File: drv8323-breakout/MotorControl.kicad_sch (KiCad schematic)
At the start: 24 parts, among them U1 DRV8323HRTAR, U2 CSD18534Q5A, U3 CSD18534Q5A, U4 CSD18534Q5A, U5 CSD18534Q5A, U6 CSD18534Q5A, U7 CSD18534Q5A

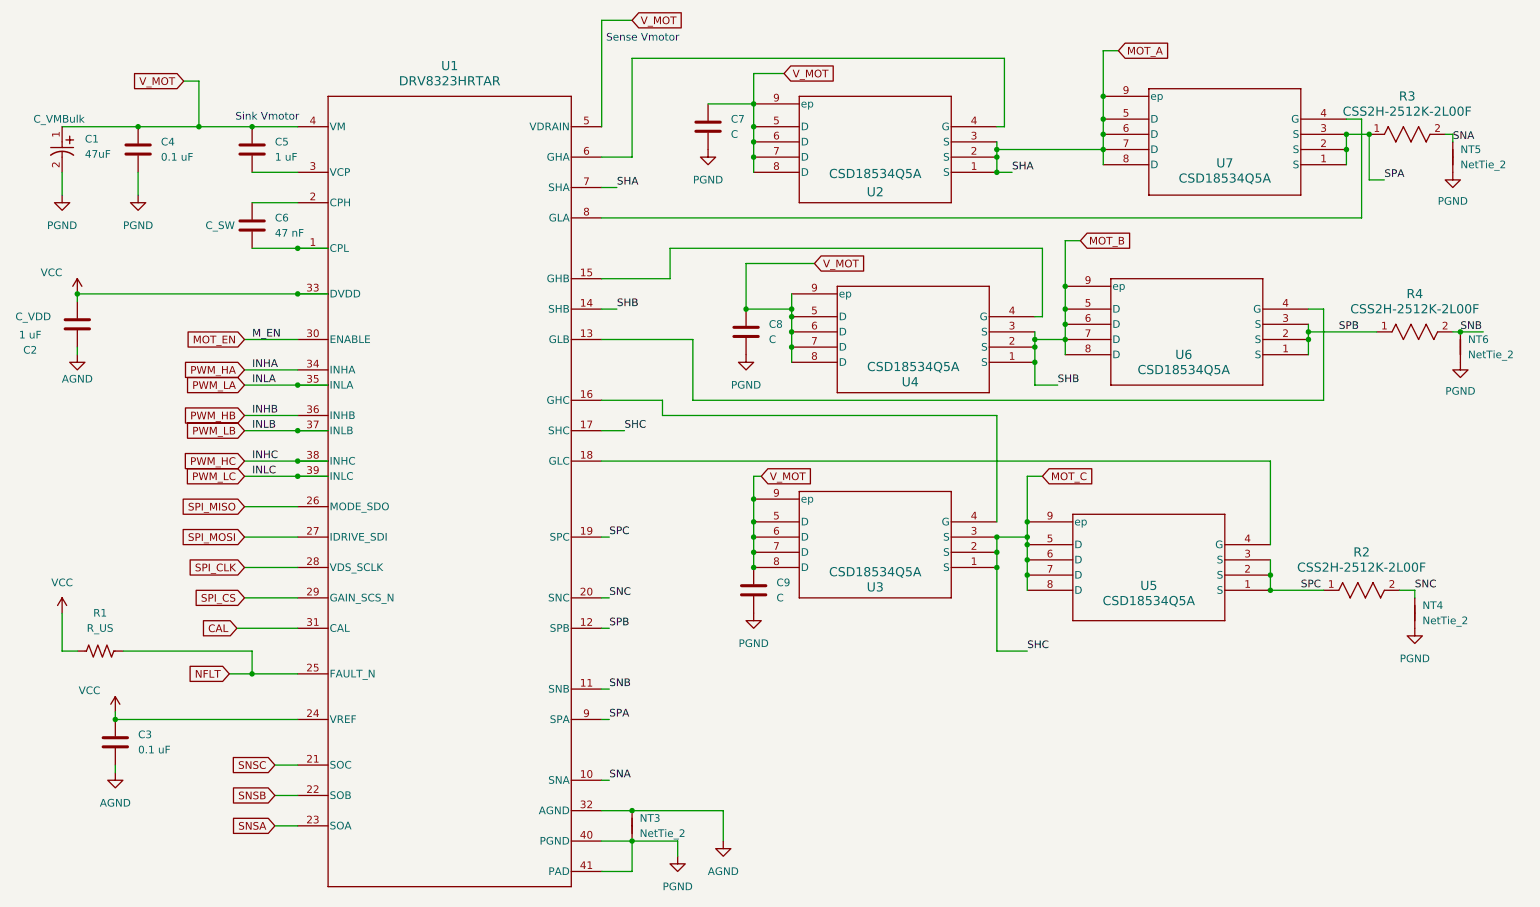
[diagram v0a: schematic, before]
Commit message: updated symbols for sanity and PCB for mfg, no DRC errors, only net type ERC errors
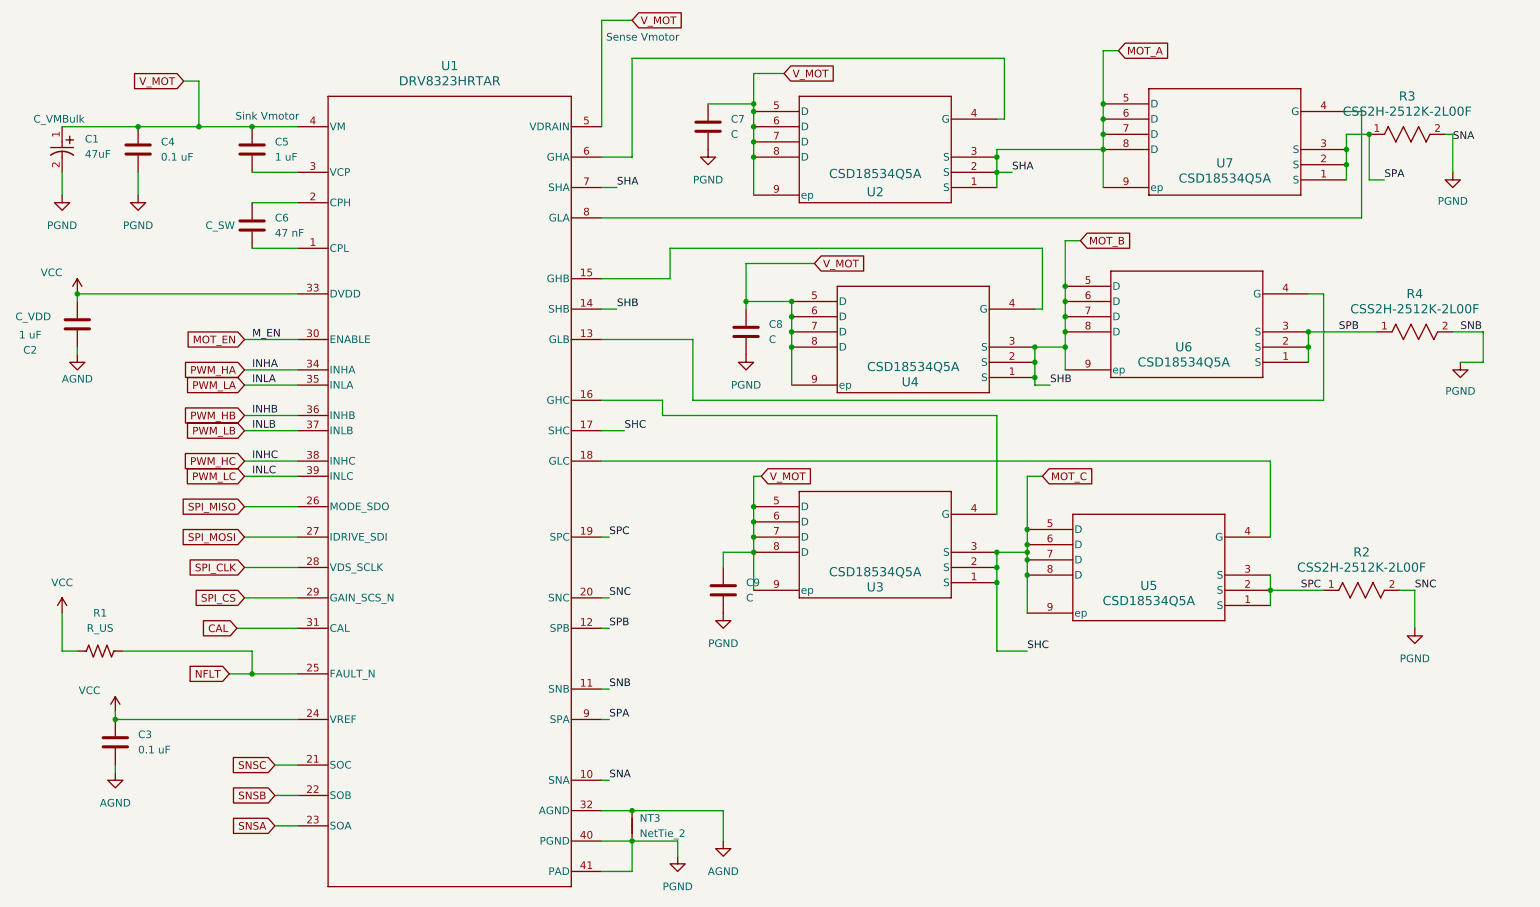
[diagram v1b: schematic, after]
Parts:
- removed NT4, NT5, NT6: NetTie_2, symbol Device:NetTie_2
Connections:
- net SNA is gone; now on net PGND: R3.2, U1.10 (SNA)
- net SNB is gone; now on net PGND: R4.2, U1.11 (SNB)
- net SNC is gone; now on net PGND: R2.2, U1.20 (SNC)
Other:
- moved on the sheet: C9, U2, U3, U4, U5, U6, U7
